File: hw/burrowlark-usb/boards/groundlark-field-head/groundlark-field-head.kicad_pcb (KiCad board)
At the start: 4 copper layers, 70 x 45 mm, 31 parts, among them J1 USB-C DEVICE, J2 SWD / 3V3 SENSE, J3 BOOT0 jumper, U1 STM32F042K6T6, U2 RM3100 XYZ, U4 AP2112K-3.3, U5 TPS22919, U6 SHT45

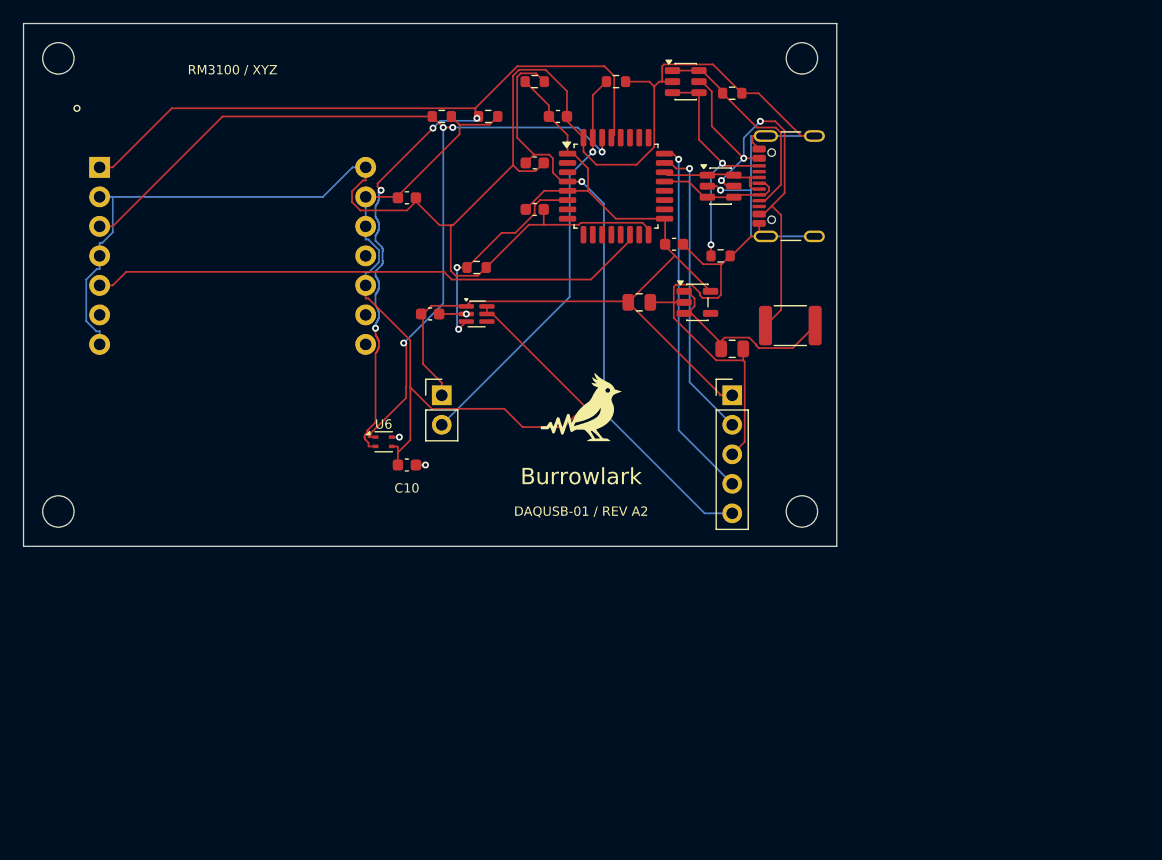
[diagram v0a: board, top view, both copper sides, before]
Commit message: Implement Burrowlark B1 four-sensor magnetic array
Use four aligned RM3100 modules on a 30 mm grid with a common SPI trigger, independent data/DRDY lanes and preserved raw cohort timing. Add explicit calibrated averaging, quartet backpressure handling, firmware fault fixtures and the matching workbench/README model.

Keep physical USB, timing, cross-talk and noise qualification explicit. The full-suite DAQHAT assembly failures are reproduced on the unchanged baseline.
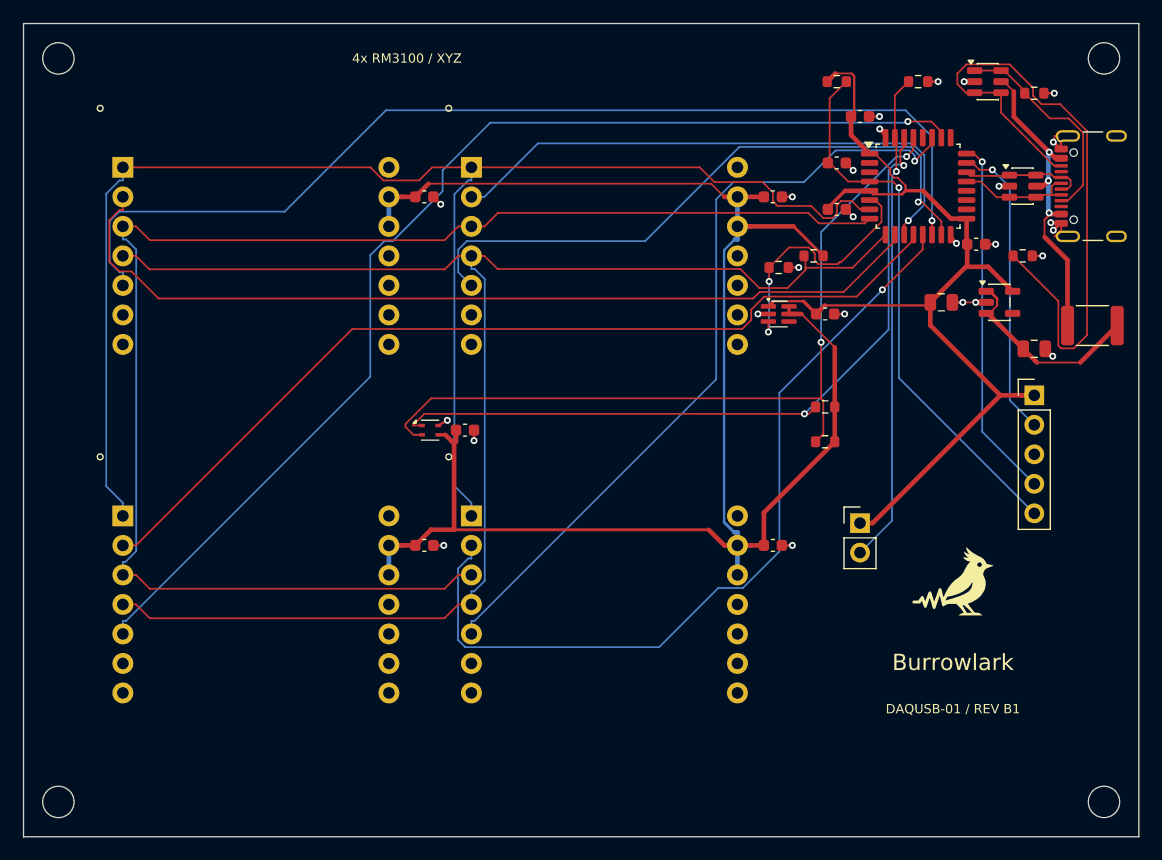
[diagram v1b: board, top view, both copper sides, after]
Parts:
- added C11: 100n, Groundlark:Capacitor_SMD__C_0603_1608Metric, F.Cu at (114.5, 64.9)
- added C12: 100n, Groundlark:Capacitor_SMD__C_0603_1608Metric, F.Cu at (84.5, 94.9)
- added C13: 100n, Groundlark:Capacitor_SMD__C_0603_1608Metric, F.Cu at (114.5, 94.9)
- added R9: 100k, Groundlark:Resistor_SMD__R_0603_1608Metric, F.Cu at (118.0, 70.0)
- added U7: RM3100 XYZ / 1, Groundlark:Groundlark__PNI_14190_Module, F.Cu at (100.0, 70.0)
- added U8: RM3100 XYZ / 2, Groundlark:Groundlark__PNI_14190_Module, F.Cu at (70.0, 100.0)
- added U9: RM3100 XYZ / 3, Groundlark:Groundlark__PNI_14190_Module, F.Cu at (100.0, 100.0)
- U2: value RM3100 XYZ -> RM3100 XYZ / 0
- moved R7 41.4 mm to (119.0, 83.0)
- moved R8 40.3 mm to (119.0, 86.0)
- moved J3 37.6 mm to (122.0, 93.0)
- moved H4 36.1 mm to (143.0, 117.0)
- moved C9 34.0 mm to (119.0, 75.0)
- moved C1 26.0 mm to (137.0, 78.0)
- moved C2 26.0 mm to (129.0, 74.0)
- moved C3 26.0 mm to (122.0, 58.0)
- moved C6 26.0 mm to (132.0, 69.0)
- moved C7 26.0 mm to (120.0, 66.0)
- moved C8 26.0 mm to (120.0, 62.0)
- moved D1 26.0 mm to (136.0, 64.0)
- moved D2 26.0 mm to (133.0, 55.0)
- moved F1 26.0 mm to (142.0, 76.0)
- moved H2 26.0 mm to (143.0, 53.0)
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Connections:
- net MAG_DRDY renamed MAG_DRDY0
- U1 pad 10: 10 -> MAG_MISO0
- U1 pad 11: 11 -> MAG_MISO1
- U1 pad 12: 12 -> MAG_MISO2
- U1 pad 13: 13 -> MAG_MISO3
- U1 pad 15: 15 -> MAG_DRDY1
- U1 pad 26: 26 -> MAG_DRDY2
- U1 pad 27: 27 -> MAG_DRDY3
- U1 pad 7: 7 -> MAG_SCK
- U1 pad 8: 8 -> MAG_MOSI
- U1 pad 9: 9 -> MAG_CSN
- U2 pad 1: SCL -> MAG_SCK
- U2 pad 10: V3_SENSOR -> GND
- U2 pad 11: u2-11 -> 11
- U2 pad 2: GND -> MAG_MISO0
- U2 pad 3: SDA -> MAG_MOSI
- U2 pad 4: GND -> MAG_CSN
- U2 pad 8: u2-8 -> 8
- U2 pad 9: u2-9 -> 9
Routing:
- net GND: track 210.9 -> 32.2 mm, vias 4 -> 27
- net MAG_CSN: track 0.00 -> 133.1 mm
- net MAG_SCK: track 0.00 -> 131.5 mm
- net MAG_MOSI: track 0.00 -> 128.5 mm
- net MAG_DRDY2: track 0.00 -> 97.4 mm, vias 0 -> 1
- net MAG_MISO2: track 0.00 -> 79.9 mm
- net MAG_MISO0: track 0.00 -> 77.7 mm
- net V3_SENSOR: track 72.8 -> 149.6 mm
- net MAG_MISO3: track 0.00 -> 72.5 mm, vias 0 -> 1
- net MAG_DRDY3: track 0.00 -> 68.4 mm, vias 0 -> 1
- net MAG_DRDY1: track 0.00 -> 55.2 mm, vias 0 -> 1
- net MAG_MISO1: track 0.00 -> 48.9 mm, vias 0 -> 1
- net MAG_DRDY0: track 48.3 -> 90.3 mm, vias 0 -> 1
- net USB_CC2: track 20.8 -> 58.0 mm, vias 2 -> 0
- net SCL: track 91.4 -> 69.0 mm, vias 4 -> 2
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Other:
- board size 70 x 45 mm -> 96 x 70 mm
- board text added: "4x RM3100 / XYZ"
- board text added: "DAQUSB-01 / REV B1"
- board text removed: "DAQUSB-01 / REV A2"
- board text removed: "RM3100 / XYZ"
